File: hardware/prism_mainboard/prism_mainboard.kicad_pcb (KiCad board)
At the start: 6 copper layers, 6 parts, among them U1 XC7Z015-2CLG485I, U2 LMS7002M, U4 AMS1117-1.8, U5 AMS1117-1.8, U6 AMS1117-1.8, U7 AMS1117-1.8

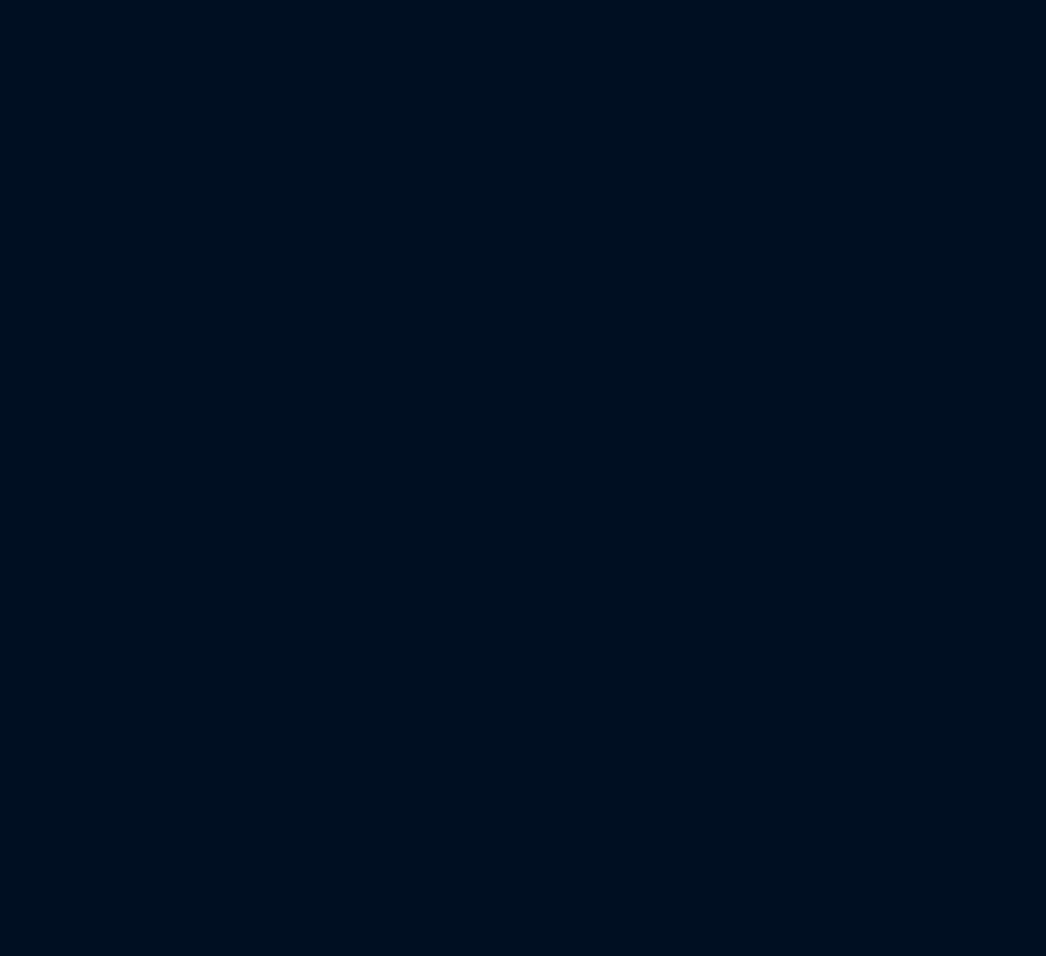
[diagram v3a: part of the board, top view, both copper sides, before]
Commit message: Updated PCB
Missing footprints due to not being properly loaded on this version, will update on other PC to consolidate layout. Will work on DDR3 lines to Zynq-7000 Processing System Next.
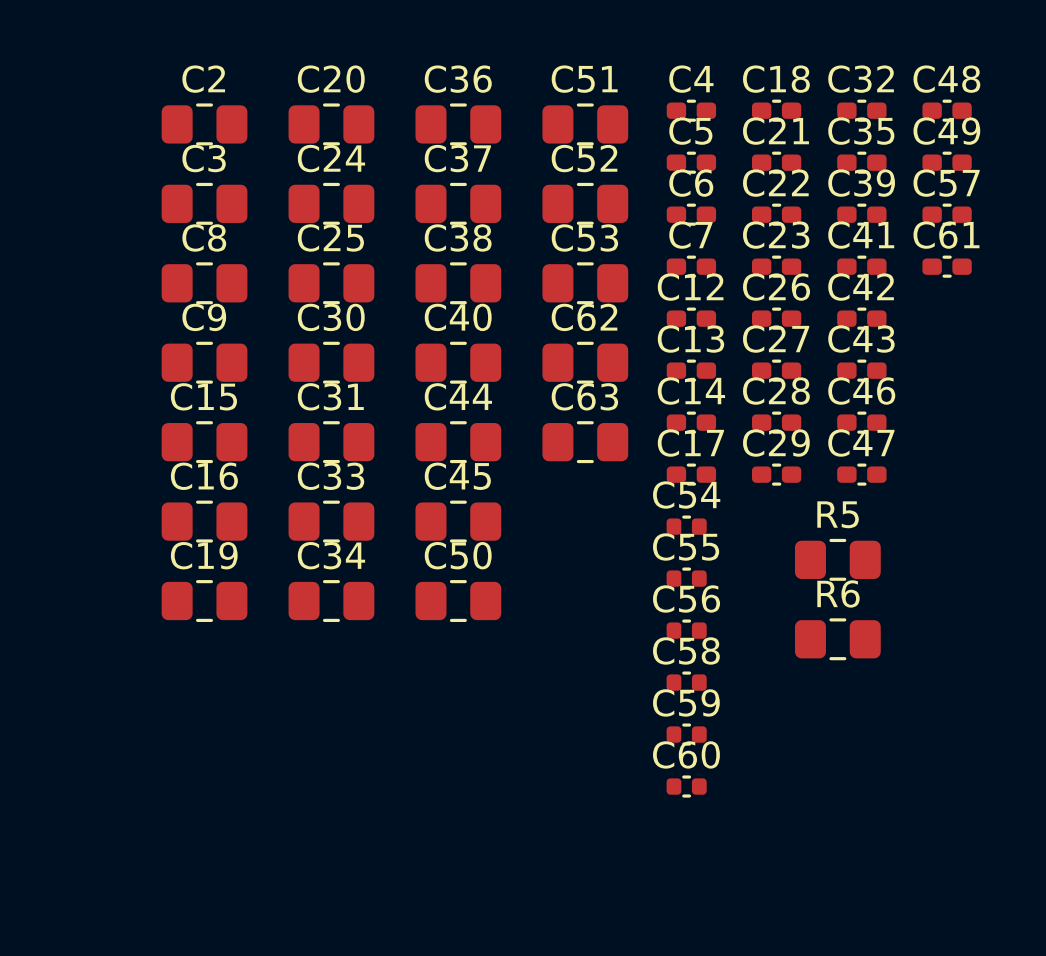
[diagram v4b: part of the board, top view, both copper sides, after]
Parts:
- added C12: 470nF, Capacitor_SMD:C_0402_1005Metric_Pad0.74x0.62mm_HandSolder, F.Cu at (230.4, 69.4)
- added C13: 470nF, Capacitor_SMD:C_0402_1005Metric_Pad0.74x0.62mm_HandSolder, F.Cu at (230.4, 71.3)
- added C14: 470nF, Capacitor_SMD:C_0402_1005Metric_Pad0.74x0.62mm_HandSolder, F.Cu at (230.4, 73.3)
- added C15: 47uF, Capacitor_SMD:C_0805_2012Metric_Pad1.18x1.45mm_HandSolder, F.Cu at (211.9, 74.0)
- added C16: 4.7uF, Capacitor_SMD:C_0805_2012Metric_Pad1.18x1.45mm_HandSolder, F.Cu at (211.9, 77.1)
- added C17: 470nF, Capacitor_SMD:C_0402_1005Metric_Pad0.74x0.62mm_HandSolder, F.Cu at (230.4, 75.3)
- added C18: 470nF, Capacitor_SMD:C_0402_1005Metric_Pad0.74x0.62mm_HandSolder, F.Cu at (233.6, 61.5)
- added C19: 47uF, Capacitor_SMD:C_0805_2012Metric_Pad1.18x1.45mm_HandSolder, F.Cu at (211.9, 80.1)
- added C2: 4.7uF, Capacitor_SMD:C_0805_2012Metric_Pad1.18x1.45mm_HandSolder, F.Cu at (211.9, 62.0)
- added C20: 4.7uF, Capacitor_SMD:C_0805_2012Metric_Pad1.18x1.45mm_HandSolder, F.Cu at (216.7, 62.0)
- added C21: 470nF, Capacitor_SMD:C_0402_1005Metric_Pad0.74x0.62mm_HandSolder, F.Cu at (233.6, 63.5)
- added C22: 470nF, Capacitor_SMD:C_0402_1005Metric_Pad0.74x0.62mm_HandSolder, F.Cu at (233.6, 65.4)
- added C23: 470nF, Capacitor_SMD:C_0402_1005Metric_Pad0.74x0.62mm_HandSolder, F.Cu at (233.6, 67.4)
- added C24: 100uF, Capacitor_SMD:C_0805_2012Metric_Pad1.18x1.45mm_HandSolder, F.Cu at (216.7, 65.0)
- added C25: 4.7uF, Capacitor_SMD:C_0805_2012Metric_Pad1.18x1.45mm_HandSolder, F.Cu at (216.7, 68.0)
- added C26: 470nF, Capacitor_SMD:C_0402_1005Metric_Pad0.74x0.62mm_HandSolder, F.Cu at (233.6, 69.4)
- added C27: 470nF, Capacitor_SMD:C_0402_1005Metric_Pad0.74x0.62mm_HandSolder, F.Cu at (233.6, 71.3)
- added C28: 470nF, Capacitor_SMD:C_0402_1005Metric_Pad0.74x0.62mm_HandSolder, F.Cu at (233.6, 73.3)
- added C29: 470nF, Capacitor_SMD:C_0402_1005Metric_Pad0.74x0.62mm_HandSolder, F.Cu at (233.6, 75.3)
- added C3: 4.7uF, Capacitor_SMD:C_0805_2012Metric_Pad1.18x1.45mm_HandSolder, F.Cu at (211.9, 65.0)
- added C30: 100uF, Capacitor_SMD:C_0805_2012Metric_Pad1.18x1.45mm_HandSolder, F.Cu at (216.7, 71.0)
- added C31: 4.7uF, Capacitor_SMD:C_0805_2012Metric_Pad1.18x1.45mm_HandSolder, F.Cu at (216.7, 74.0)
- added C32: 470nF, Capacitor_SMD:C_0402_1005Metric_Pad0.74x0.62mm_HandSolder, F.Cu at (236.8, 61.5)
- added C33: 100uF, Capacitor_SMD:C_0805_2012Metric_Pad1.18x1.45mm_HandSolder, F.Cu at (216.7, 77.1)
- added C34: 4.7uF, Capacitor_SMD:C_0805_2012Metric_Pad1.18x1.45mm_HandSolder, F.Cu at (216.7, 80.1)
- added C35: 470nF, Capacitor_SMD:C_0402_1005Metric_Pad0.74x0.62mm_HandSolder, F.Cu at (236.8, 63.5)
- added C36: 47uF, Capacitor_SMD:C_0805_2012Metric_Pad1.18x1.45mm_HandSolder, F.Cu at (221.5, 62.0)
- added C37: 47uF, Capacitor_SMD:C_0805_2012Metric_Pad1.18x1.45mm_HandSolder, F.Cu at (221.5, 65.0)
- added C38: 4.7uF, Capacitor_SMD:C_0805_2012Metric_Pad1.18x1.45mm_HandSolder, F.Cu at (221.5, 68.0)
- added C39: 470nF, Capacitor_SMD:C_0402_1005Metric_Pad0.74x0.62mm_HandSolder, F.Cu at (236.8, 65.4)
- added C4: 470nF, Capacitor_SMD:C_0402_1005Metric_Pad0.74x0.62mm_HandSolder, F.Cu at (230.4, 61.5)
- added C40: 4.7uF, Capacitor_SMD:C_0805_2012Metric_Pad1.18x1.45mm_HandSolder, F.Cu at (221.5, 71.0)
- added C41: 470nF, Capacitor_SMD:C_0402_1005Metric_Pad0.74x0.62mm_HandSolder, F.Cu at (236.8, 67.4)
- added C42: 470nF, Capacitor_SMD:C_0402_1005Metric_Pad0.74x0.62mm_HandSolder, F.Cu at (236.8, 69.4)
- added C43: 470nF, Capacitor_SMD:C_0402_1005Metric_Pad0.74x0.62mm_HandSolder, F.Cu at (236.8, 71.3)
- added C44: 4.7uF, Capacitor_SMD:C_0805_2012Metric_Pad1.18x1.45mm_HandSolder, F.Cu at (221.5, 74.0)
- added C45: 4.7uF, Capacitor_SMD:C_0805_2012Metric_Pad1.18x1.45mm_HandSolder, F.Cu at (221.5, 77.1)
- added C46: 470nF, Capacitor_SMD:C_0402_1005Metric_Pad0.74x0.62mm_HandSolder, F.Cu at (236.8, 73.3)
- added C47: 470nF, Capacitor_SMD:C_0402_1005Metric_Pad0.74x0.62mm_HandSolder, F.Cu at (236.8, 75.3)
- added C48: 470nF, Capacitor_SMD:C_0402_1005Metric_Pad0.74x0.62mm_HandSolder, F.Cu at (240.0, 61.5)
- added C49: 470nF, Capacitor_SMD:C_0402_1005Metric_Pad0.74x0.62mm_HandSolder, F.Cu at (240.0, 63.5)
- added C5: 470nF, Capacitor_SMD:C_0402_1005Metric_Pad0.74x0.62mm_HandSolder, F.Cu at (230.4, 63.5)
- added C50: 1uF, Capacitor_SMD:C_0805_2012Metric_Pad1.18x1.45mm_HandSolder, F.Cu at (221.5, 80.1)
- added C51: 1uF, Capacitor_SMD:C_0805_2012Metric_Pad1.18x1.45mm_HandSolder, F.Cu at (226.3, 62.0)
- added C52: 1uF, Capacitor_SMD:C_0805_2012Metric_Pad1.18x1.45mm_HandSolder, F.Cu at (226.3, 65.0)
- added C53: 1uF, Capacitor_SMD:C_0805_2012Metric_Pad1.18x1.45mm_HandSolder, F.Cu at (226.3, 68.0)
- added C54: 0.1uF, Capacitor_SMD:C_0402_1005Metric, F.Cu at (230.2, 77.2)
- added C55: 0.1uF, Capacitor_SMD:C_0402_1005Metric, F.Cu at (230.2, 79.2)
- added C56: 10nF, Capacitor_SMD:C_0402_1005Metric, F.Cu at (230.2, 81.2)
- added C57: 10nF, Capacitor_SMD:C_0402_1005Metric_Pad0.74x0.62mm_HandSolder, F.Cu at (240.0, 65.4)
- added C58: 0.1uF, Capacitor_SMD:C_0402_1005Metric, F.Cu at (230.2, 83.2)
- added C59: 0.1uF, Capacitor_SMD:C_0402_1005Metric, F.Cu at (230.2, 85.1)
- added C6: 470nF, Capacitor_SMD:C_0402_1005Metric_Pad0.74x0.62mm_HandSolder, F.Cu at (230.4, 65.4)
- added C60: 0.1uF, Capacitor_SMD:C_0402_1005Metric, F.Cu at (230.2, 87.1)
- added C61: 4.7uF, Capacitor_SMD:C_0402_1005Metric_Pad0.74x0.62mm_HandSolder, F.Cu at (240.0, 67.4)
- added C62: 47uF, Capacitor_SMD:C_0805_2012Metric_Pad1.18x1.45mm_HandSolder, F.Cu at (226.3, 71.0)
- added C63: 47uF, Capacitor_SMD:C_0805_2012Metric_Pad1.18x1.45mm_HandSolder, F.Cu at (226.3, 74.0)
- added C7: 470nF, Capacitor_SMD:C_0402_1005Metric_Pad0.74x0.62mm_HandSolder, F.Cu at (230.4, 67.4)
- added C8: 100uF, Capacitor_SMD:C_0805_2012Metric_Pad1.18x1.45mm_HandSolder, F.Cu at (211.9, 68.0)
- added C9: 4.7uF, Capacitor_SMD:C_0805_2012Metric_Pad1.18x1.45mm_HandSolder, F.Cu at (211.9, 71.0)
- added R5: 20k, Capacitor_SMD:C_0805_2012Metric_Pad1.18x1.45mm_HandSolder, F.Cu at (235.9, 78.5)
- added R6: 20k, Capacitor_SMD:C_0805_2012Metric_Pad1.18x1.45mm_HandSolder, F.Cu at (235.9, 81.5)
